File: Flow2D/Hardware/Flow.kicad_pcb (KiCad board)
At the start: 2 copper layers, 50 x 50 mm, 51 parts, among them J1 Conn_02x05_Odd_Even, U1 SN74LVC2G17, U2 LR9102G, U3 TLV9064IDR, U4 STM32G030F6Px

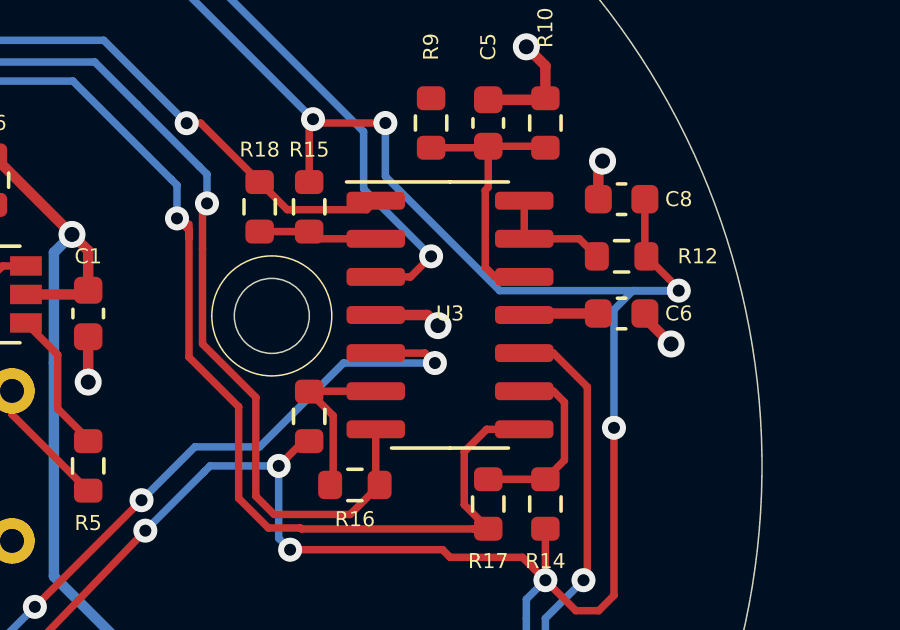
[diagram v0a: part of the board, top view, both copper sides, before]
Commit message: Problems related to firmware are solved.
TODO:
+Signal level is too low; like 200mV. Need to be increased.
+Need to be tested with a plastic ring.
+Piezodriver units response is unknown, need to be determined.
+A bit more calculation about vectors required.
+No need for making DMA of the TIM1 active, could be deactivated.
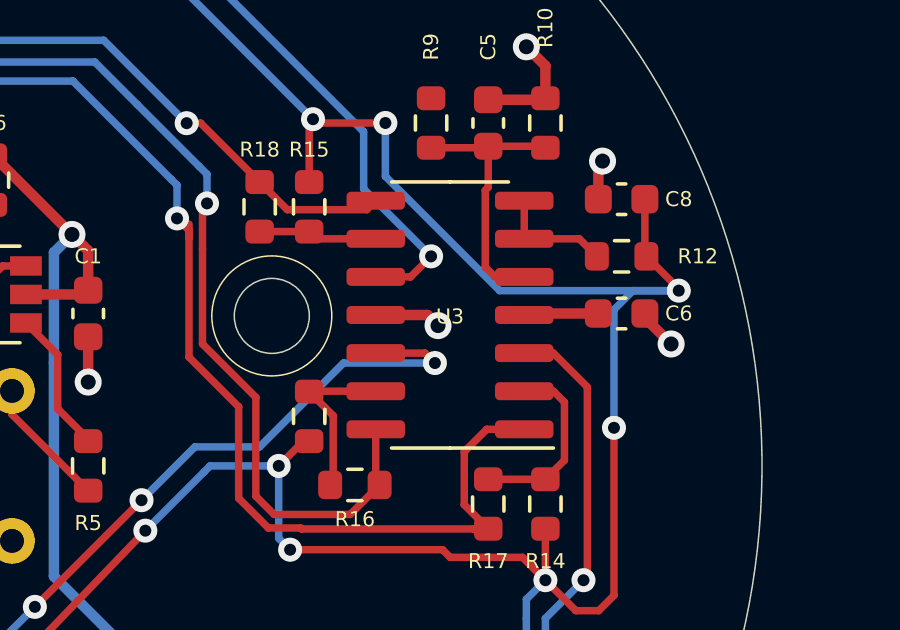
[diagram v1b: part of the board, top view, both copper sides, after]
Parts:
- turned U3 to 180 degrees
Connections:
- U3 pad 1: Net-(R18-Pad2) -> Net-(R17-Pad2)
- U3 pad 10: /SIGNAL_C -> /SIGNAL_A
- U3 pad 11: VDD -> GND
- U3 pad 12: Net-(C5-Pad1) -> /SIGNAL_B
- U3 pad 13: Net-(R12-Pad2) -> Net-(R13-Pad1)
- U3 pad 14: Net-(R12-Pad2) -> Net-(R16-Pad2)
- U3 pad 2: Net-(R15-Pad1) -> Net-(R14-Pad1)
- U3 pad 3: /SIGNAL_A -> /SIGNAL_C
- U3 pad 4: GND -> VDD
- U3 pad 5: /SIGNAL_B -> Net-(C5-Pad1)
- U3 pad 6: Net-(R13-Pad1) -> Net-(R12-Pad2)
- U3 pad 7: Net-(R16-Pad2) -> Net-(R12-Pad2)
- U3 pad 8: Net-(R17-Pad2) -> Net-(R18-Pad2)
- U3 pad 9: Net-(R14-Pad1) -> Net-(R15-Pad1)
